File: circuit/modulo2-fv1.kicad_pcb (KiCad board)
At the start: 2 copper layers, 107 x 48 mm, 2 parts, among them J4 HOLE, J5 HOLE

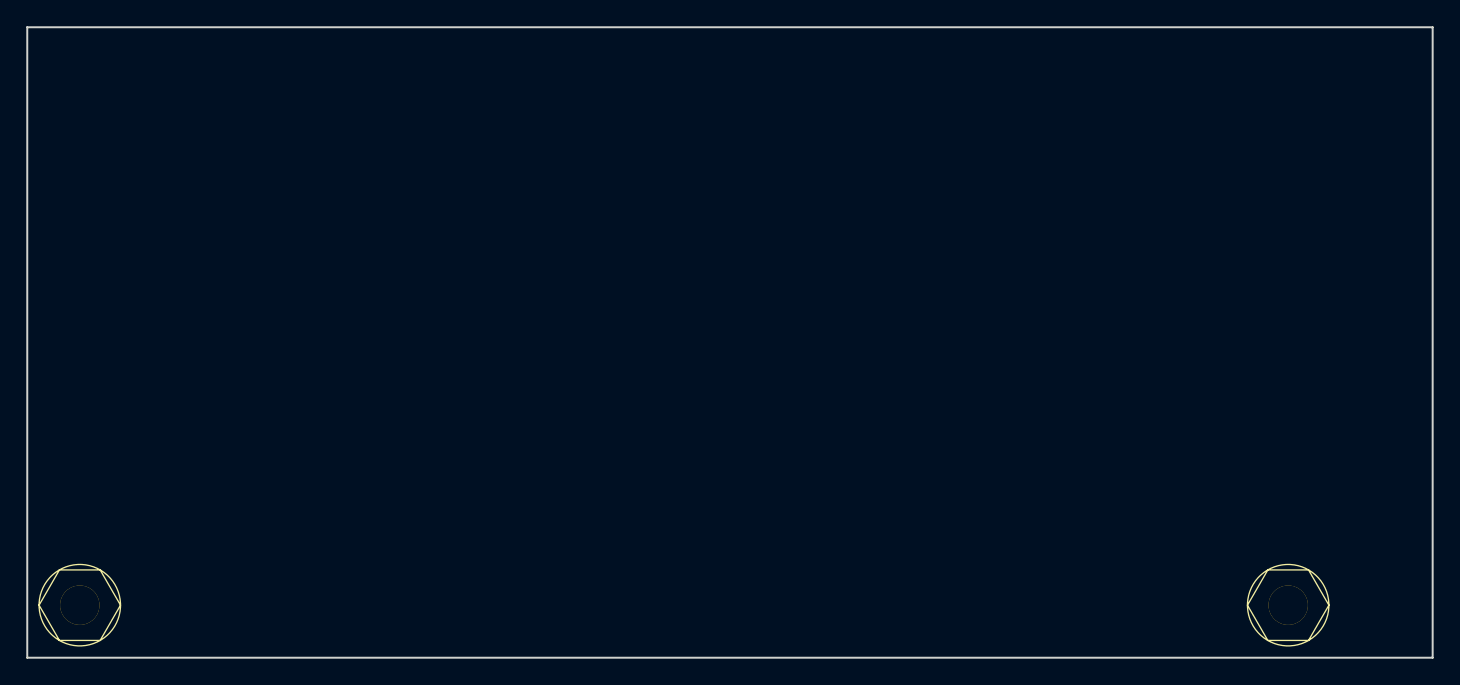
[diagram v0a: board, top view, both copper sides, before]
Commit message: made FV-1 prototype; converted kicad 5 files to kicad 6
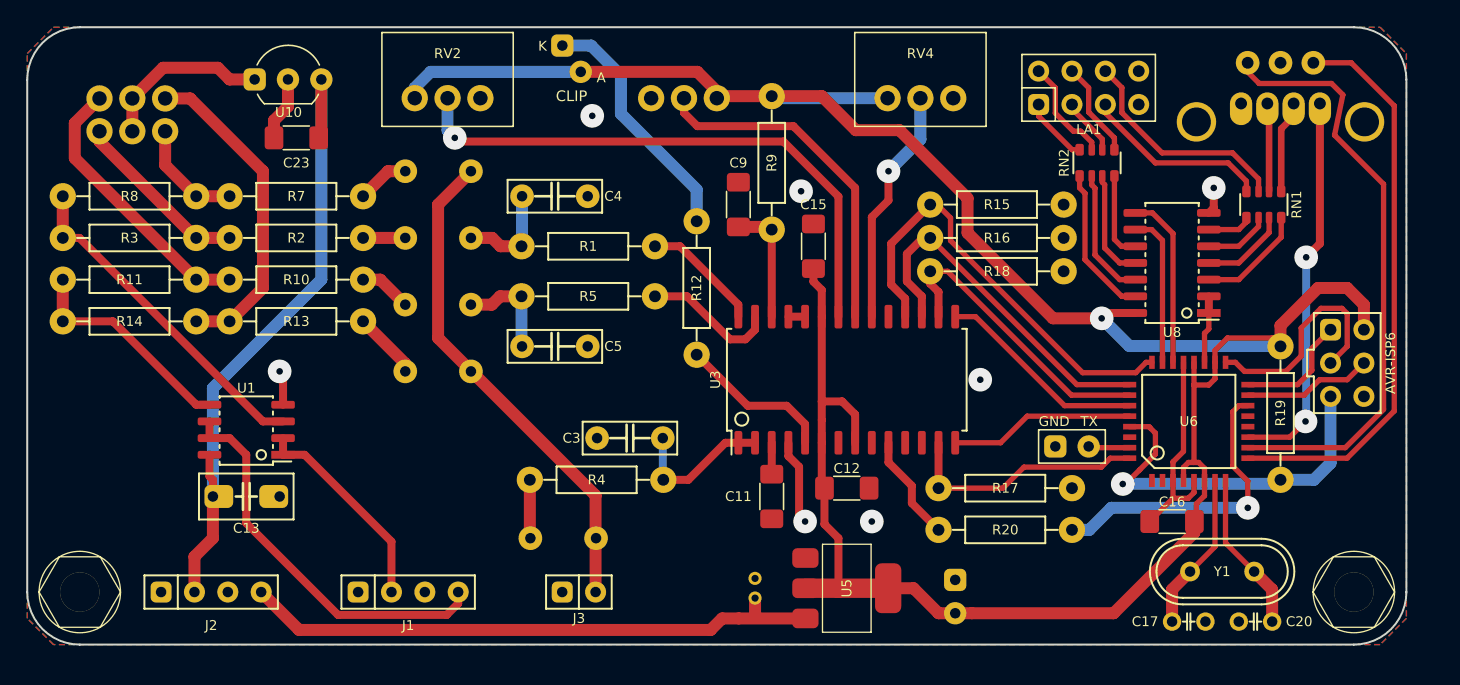
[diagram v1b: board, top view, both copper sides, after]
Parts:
- added C1: 1µF, myAmp:C_FILM_L7.2mm_W4.5mm_P5.00mm, B.Cu at (81.3, 66.0)
- added C10: 1µF, myAmp:C_FILM_L7.2mm_W4.5mm_P5.00mm, B.Cu at (81.3, 71.1)
- added C11: 1µF, myAmp:C_1206, F.Cu at (106.7, 85.7)
- added C12: 100nF, myAmp:C_1206, F.Cu at (112.4, 85.1)
- added C13: 100nF, myAmp:C_5MM_1206, F.Cu at (66.7, 85.7)
- added C14: 1µF, myAmp:C_FILM_L7.2mm_W4.5mm_P5.00mm, B.Cu at (81.3, 76.2)
- added C15: 100nF, myAmp:C_1206, F.Cu at (109.9, 66.7)
- added C16: 100n, myAmp:C_1206, F.Cu at (137.2, 87.6)
- added C17: 22p, myAmp:C_2.5MM, F.Cu at (138.4, 95.2)
- added C18: 10µF, myAmp:CPOL_D4_P1.5, B.Cu at (105.4, 92.7)
- added C19: 100µF, myAmp:CPOL_D6.3_P2.5, B.Cu at (120.7, 93.3)
- added C2: 1µF, myAmp:C_FILM_L7.2mm_W4.5mm_P5.00mm, B.Cu at (90.8, 88.9)
- added C20: 22p, myAmp:C_2.5MM, F.Cu at (143.5, 95.2)
- added C23: 100nF, myAmp:C_1206, F.Cu at (70.5, 58.4)
- added C3: 1nF, myAmp:C_FILM_L7.2mm_W2.5mm_P5.00mm, F.Cu at (95.9, 81.3)
- added C4: 10nF, myAmp:C_FILM_L7.2mm_W2.5mm_P5.00mm, F.Cu at (90.2, 62.9)
- added C5: 10nF, myAmp:C_FILM_L7.2mm_W2.5mm_P5.00mm, F.Cu at (90.2, 74.3)
- added C7: 1µF, myAmp:C_FILM_L7.2mm_W4.5mm_P5.00mm, B.Cu at (81.3, 61.0)
- added C9: 1µF, myAmp:C_1206, F.Cu at (104.1, 63.5)
- added D1: CLIP, myAmp:LED_D3.0mm_PCBedge, F.Cu at (91.4, 50.4)
- added J1: CONN_01X04, myAmp:PIN_1x04, F.Cu at (79.0, 93.0)
- added J2: CONN_01X04, myAmp:PIN_1x04, F.Cu at (64.0, 93.0)
- added J3: CONN_01X02, myAmp:PIN_1x02, F.Cu at (92.0, 93.0)
- added LA1: LED_ARRAY, myAmp:LED_ARRAY, F.Cu at (130.8, 54.6)
- added R1: 1K, myAmp:R_10MM, F.Cu at (92.7, 66.7)
- added R10: 10K, myAmp:R_10MM, F.Cu at (70.5, 69.2)
- added R11: 10K, myAmp:R_10MM, F.Cu at (57.8, 69.2)
- added R12: 100, myAmp:R_10MM, F.Cu at (101.0, 69.8)
- added R13: 10K, myAmp:R_10MM, F.Cu at (70.5, 72.4)
- added R14: 10K, myAmp:R_10MM, F.Cu at (57.8, 72.4)
- added R15: 10K, myAmp:R_10MM, F.Cu at (123.8, 63.5)
- added R16: 10K, myAmp:R_10MM, F.Cu at (123.8, 66.0)
- added R17: 10K, myAmp:R_10MM, F.Cu at (124.5, 85.1)
- added R18: 10K, myAmp:R_10MM, F.Cu at (123.8, 68.6)
- added R19: 10K, myAmp:R_10MM, F.Cu at (145.4, 79.4)
- added R2: 10K, myAmp:R_10MM, F.Cu at (70.5, 66.0)
- added R20: 10K, myAmp:R_10MM, F.Cu at (124.5, 88.3)
- added R3: 10K, myAmp:R_10MM, F.Cu at (57.8, 66.0)
- added R4: 1K, myAmp:R_10MM, F.Cu at (93.3, 84.5)
- added R5: 1K, myAmp:R_10MM, F.Cu at (92.7, 70.5)
- added R7: 10K, myAmp:R_10MM, F.Cu at (70.5, 62.9)
- added R8: 10K, myAmp:R_10MM, F.Cu at (57.8, 62.9)
- added R9: 100, myAmp:R_10MM, F.Cu at (106.7, 60.3)
- added RN1: 100, myAmp:R_Array_x4_1206, F.Cu at (144.1, 63.5)
- added RN2: 100, myAmp:R_Array_x4_1206, F.Cu at (131.4, 60.3)
- added RV1: B10K, myAmp:BOURNS_PTD902_xx15K, B.Cu at (58.0, 57.9)
- added RV2: 50K, myAmp:BOURNS_PTD901_xx15K, F.Cu at (82.0, 55.4)
- added RV3: 50K, myAmp:BOURNS_PTD901_xx15K, B.Cu at (100.0, 55.4)
- added RV4: 50K, myAmp:BOURNS_PTD901_xx15K, F.Cu at (118.0, 55.4)
- added SW1: ROTENC_BOURNS_PEL12D, myAmp:BOURNS_PEL12D-2xxx, B.Cu at (145.4, 52.7)
- added U1: NE5532, myAmp:SOIC-8_3.9x4.9mm_P1.27mm, F.Cu at (66.7, 80.6)
- added U10: TLE2426, myAmp:TO-92_Inline_Wide, F.Cu at (69.8, 54.0)
- added U3: FV-1, myAmp:SOIC-28_7.5x17.9mm_Pitch1.27mm, F.Cu at (112.4, 76.8)
- added U4: AVR-ISP6, myAmp:AVR_ISP6, F.Cu at (150.5, 75.6)
- added U5: LM1117 3V3, myAmp:SOT-223, F.Cu at (112.4, 92.7)
- added U6: ATmega328p, myAmp:TQFP-32_7x7mm_Pitch0.8mm, F.Cu at (138.4, 80.0)
- added U7: DBG_UART, myAmp:DBG_UART, F.Cu at (129.5, 81.9)
- added U8: 74164, myAmp:SOIC-14_3.9x8.7mm_P1.27mm, F.Cu at (137.2, 67.9)
- added Y1: 16MHz, myAmp:Crystal_HC49-U_Vertical, F.Cu at (141.0, 91.4)
- moved J4 5.10 mm to (151.0, 93.0)
- moved J5 1.00 mm to (54.0, 93.0)
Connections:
- J4 pad 1: (no net) -> unconnected-(J4-Pad1)
- J5 pad 1: (no net) -> unconnected-(J5-Pad1)
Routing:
- net +3V3: track 0.00 -> 189.6 mm, vias 0 -> 1
- net +24V: track 0.00 -> 50.8 mm
- net /ROT_A: track 0.00 -> 45.8 mm
- net +5V: track 0.00 -> 44.5 mm
- net Net-(RV2-Pad2): track 0.00 -> 43.5 mm, vias 0 -> 1
- net /ROT_B: track 0.00 -> 43.4 mm
- net IN: track 0.00 -> 38.1 mm
- net /S2: track 0.00 -> 33.7 mm
- net GND: track 0.00 -> 33.3 mm, vias 0 -> 7
- net /OUTR: track 0.00 -> 30.1 mm
- net /ROT_SW: track 0.00 -> 29.5 mm, vias 0 -> 2
- net /AVR_RST: track 0.00 -> 28.8 mm, vias 0 -> 1
- net /S1: track 0.00 -> 27.3 mm
- net Net-(RV3-Pad2): track 0.00 -> 26.3 mm
- net Net-(R3-Pad2): track 0.00 -> 25.7 mm
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- added copper zone on B.Cu, net GND
- added copper zone on F.Cu, net GND
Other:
- board size 107 x 48 mm -> 105 x 47 mm
- net class Default removed

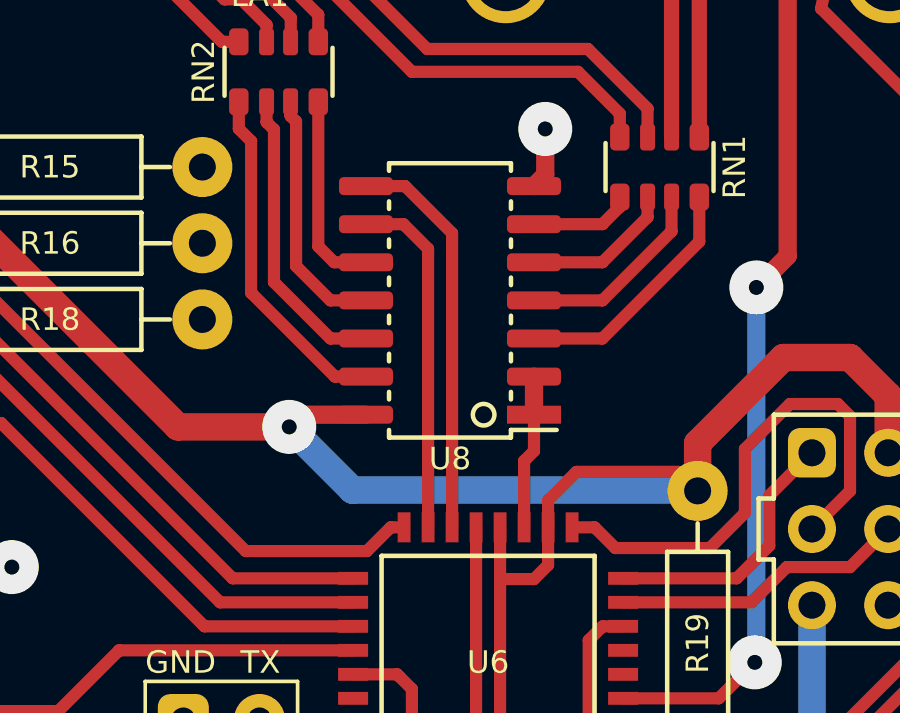
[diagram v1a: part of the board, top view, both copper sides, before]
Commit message: FV-1 firmware reworked for the new board; FV-1 PCB needs rework to correct errors
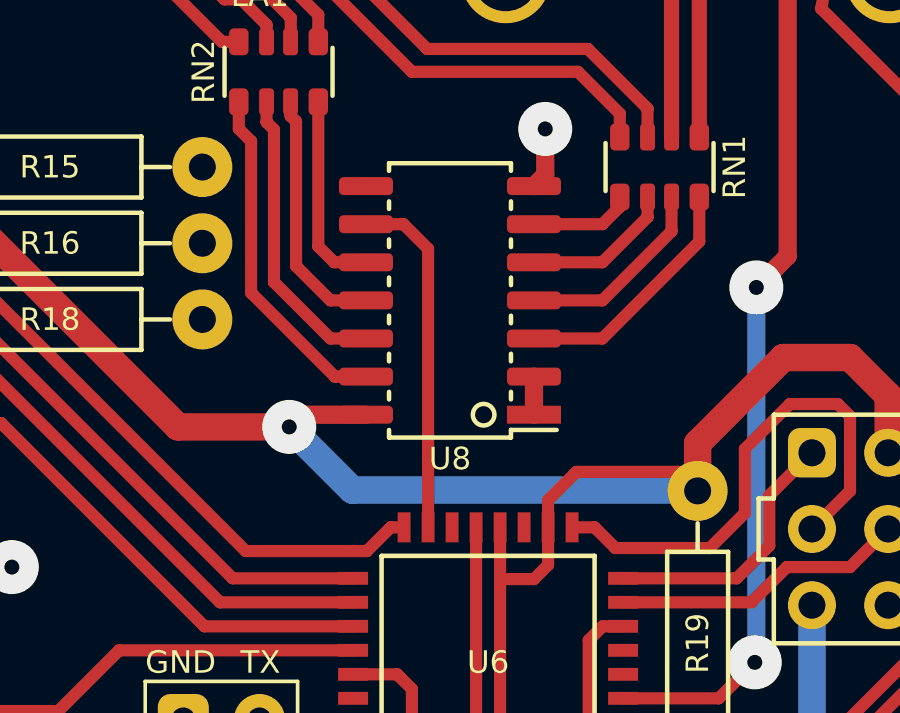
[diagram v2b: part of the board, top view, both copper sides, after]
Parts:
- C16: value 100n -> 100nF
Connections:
- U6 pad 12: unconnected-(U6-Pad12) -> /LED_CK
- U6 pad 13: unconnected-(U6-Pad13) -> /LED_DT
- U6 pad 19: /LED_DT -> unconnected-(U6-Pad19)
- U6 pad 22: /LED_CK -> unconnected-(U6-Pad22)
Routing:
- net /LED_CK: track 13.3 -> 0.00 mm
- net /LED_DT: track 5.16 -> 1.27 mm
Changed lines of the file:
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@@
   (net 62 "Net-(R20-Pad1)")
   (net 63 "unconnected-(U6-Pad1)")
-  (net 64 "unconnected-(U6-Pad12)")
-  (net 65 "unconnected-(U6-Pad13)")
+  (net 64 "unconnected-(U6-Pad19)")
+  (net 65 "unconnected-(U6-Pad22)")
   (net 66 "unconnected-(U6-Pad2)")
   (net 67 "Net-(LA1-Pad2)")
@@
       (net 48 "/ROT_SW") (pinfunction "(AIN1)PD7") (pintype "bidirectional"))
     (pad "12" smd rect (at -0.4 4.5 90) (size 0.43 1) (layers "F.Cu" "F.Paste" "F.Mask")
-      (net 64 "unconnected-(U6-Pad12)") (pinfunction "(ICP)PB0") (pintype "bidirectional+no_connect"))
+      (net 57 "/LED_CK") (pinfunction "(ICP)PB0") (pintype "bidirectional"))
     (pad "13" smd rect (at 0.4 4.5 90) (size 0.43 1) (layers "F.Cu" "F.Paste" "F.Mask")
-      (net 65 "unconnected-(U6-Pad13)") (pinfunction "(OC1A)PB1") (pintype "bidirectional+no_connect"))
+      (net 56 "/LED_DT") (pinfunction "(OC1A)PB1") (pintype "bidirectional"))
     (pad "14" smd rect (at 1.2 4.5 90) (size 0.43 1) (layers "F.Cu" "F.Paste" "F.Mask")
       (net 50 "/FV_CLK") (pinfunction "(~{SS}/OC1B)PB2") (pintype "bidirectional"))
@@
       (net 11 "+3V3") (pinfunction "AVCC") (pintype "power_in"))
     (pad "19" smd rect (at 4.5 1.2 90) (size 1 0.43) (layers "F.Cu" "F.Paste" "F.Mask")
-      (net 56 "/LED_DT") (pinfunction "ADC6") (pintype "bidirectional"))
+      (net 64 "unconnected-(U6-Pad19)") (pinfunction "ADC6") (pintype "bidirectional+no_connect"))
     (pad "20" smd rect (at 4.5 0.4 90) (size 1 0.43) (layers "F.Cu" "F.Paste" "F.Mask")
       (net 11 "+3V3") (pinfunction "AREF") (pintype "bidirectional"))
@@
       (net 5 "GND") (pinfunction "AGND") (pintype "power_in"))
     (pad "22" smd rect (at 4.5 -1.2 90) (size 1 0.43) (layers "F.Cu" "F.Paste" "F.Mask")
-      (net 57 "/LED_CK") (pinfunction "ADC7") (pintype "bidirectional"))
+      (net 65 "unconnected-(U6-Pad22)") (pinfunction "ADC7") (pintype "bidirectional+no_connect"))
     (pad "23" smd rect (at 4.5 -2 90) (size 1 0.43) (layers "F.Cu" "F.Paste" "F.Mask")
       (net 58 "/LED_RST") (pinfunction "(ADC0)PC0") (pintype "bidirectional"))
@@
       (effects (font (size 0.75 0.75) (thickness 0.15)))
     )
-    (fp_text value "100n" (at 0.0127 0.5715) (layer "Dwgs.User") hide
+    (fp_text value "100nF" (at 0.0127 0.5715) (layer "Dwgs.User") hide
       (effects (font (size 0.127 0.127) (thickness 0.001)))
     )
@@
   (segment (start 147.2118 78.01) (end 142.93 78.01) (width 0.4064) (layer "F.Cu") (net 55))
   (segment (start 151.765 75.565) (end 150.495 76.835) (width 0.4064) (layer "F.Cu") (net 55))
-  (segment (start 139.63 75.51) (end 139.63 73.2982) (width 0.4064) (layer "F.Cu") (net 56))
-  (segment (start 139.63 73.2982) (end 139.96 72.9682) (width 0.4064) (layer "F.Cu") (net 56))
   (segment (start 139.96 70.485) (end 139.96 71.755) (width 0.6096) (layer "F.Cu") (net 56))
-  (segment (start 139.96 72.9682) (end 139.96 71.755) (width 0.4064) (layer "F.Cu") (net 56))
-  (segment (start 137.23 65.7036) (end 135.6614 64.135) (width 0.4064) (layer "F.Cu") (net 57))
-  (segment (start 137.23 75.51) (end 137.23 65.7036) (width 0.4064) (layer "F.Cu") (net 57))
-  (segment (start 135.6614 64.135) (end 134.36 64.135) (width 0.4064) (layer "F.Cu") (net 57))
   (segment (start 136.43 75.51) (end 136.43 66.2244) (width 0.4064) (layer "F.Cu") (net 58))
   (segment (start 135.6106 65.405) (end 134.36 65.405) (width 0.4064) (layer "F.Cu") (net 58))

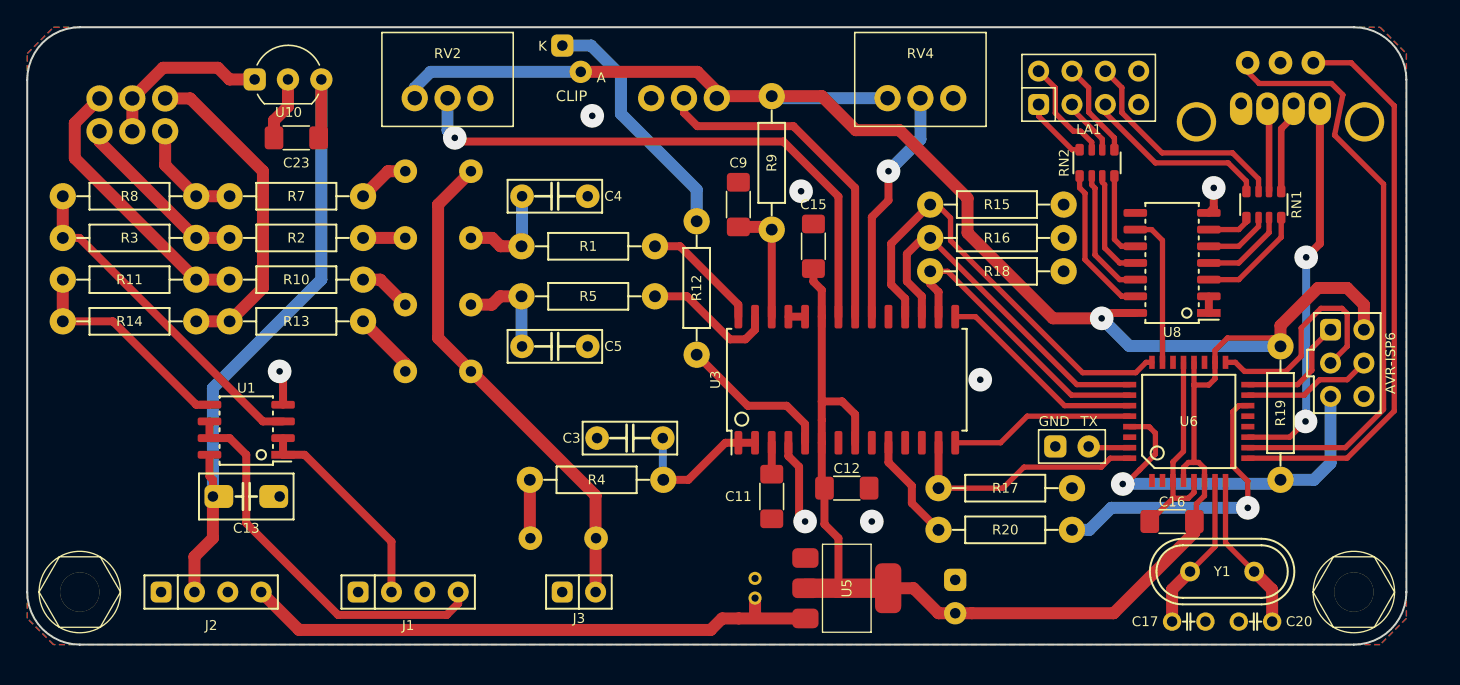
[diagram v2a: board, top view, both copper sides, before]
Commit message: added report on createBanks.py; started PCB redesign
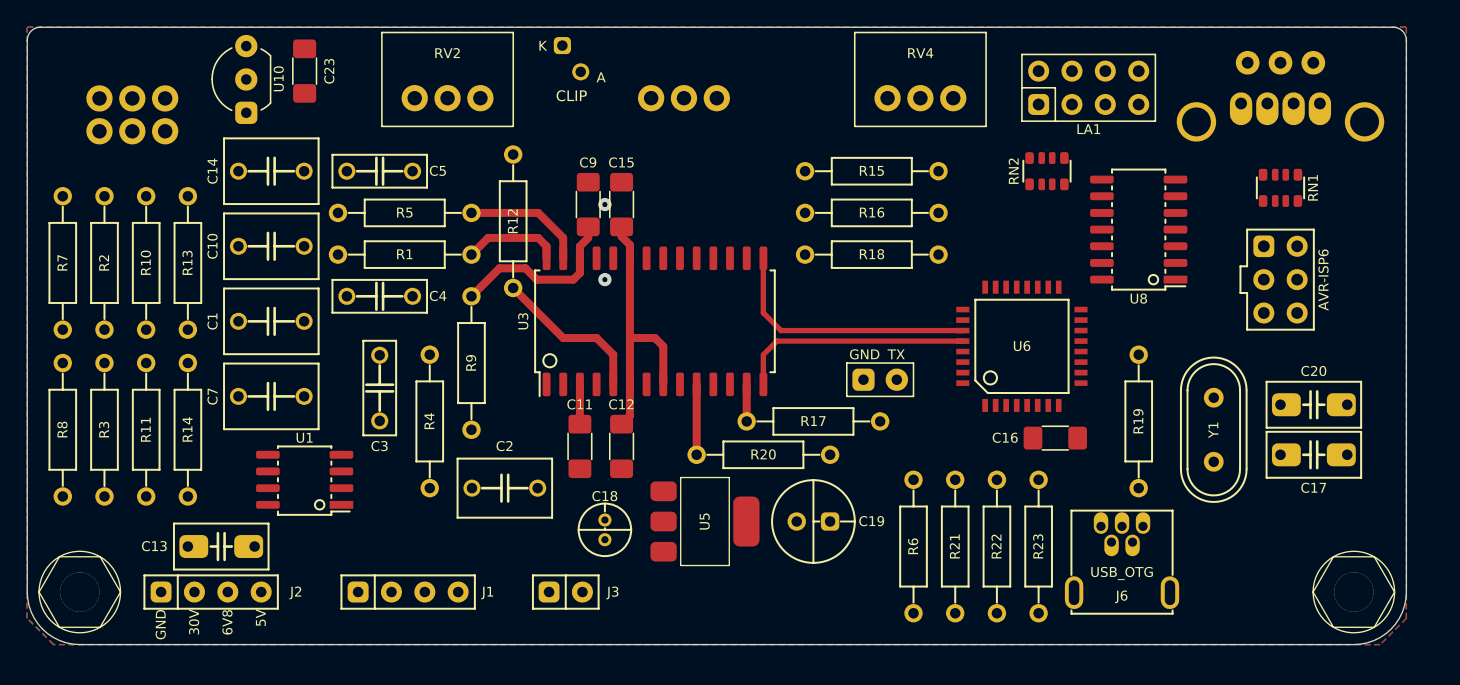
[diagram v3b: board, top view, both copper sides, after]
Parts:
- added J6: USB_OTG, myAmp:USB_OTG_THT, F.Cu at (133.3, 88.0)
- added R21: 68, myAmp:R_10MM, F.Cu at (120.7, 89.5)
- added R22: 68, myAmp:R_10MM, F.Cu at (123.8, 89.5)
- added R23: 1K5, myAmp:R_10MM, F.Cu at (127.0, 89.5)
- added R6: 1K5, myAmp:R_10MM, F.Cu at (117.5, 89.5)
- C1, C10, C14, C7: footprint myAmp:C_FILM_L7.2mm_W4.5mm_P5.00mm -> myAmp:C_FILM_L7.2mm_W5.0mm_P5.00mm; moved to F.Cu
- C17, C20: footprint myAmp:C_2.5MM -> myAmp:C_5MM_1206
- C18, C19, C2: moved to F.Cu
- J2: value CONN_01X04 -> POWER; footprint myAmp:PIN_1x04 -> myAmp:POWER
- moved R9 27.5 mm to (83.8, 75.6), turned to 90 degrees
- moved C7 21.3 mm to (68.6, 78.1)
- moved C14 19.8 mm to (68.6, 61.0)
- moved C3 19.4 mm to (76.8, 77.5), turned to 90 degrees
- moved R20 19.3 mm to (106.0, 82.5)
- moved C5 18.9 mm to (76.8, 61.0)
- moved R7 18.5 mm to (52.7, 67.9), turned to -90 degrees
- moved R8 18.5 mm to (52.7, 80.6), turned to -90 degrees
- moved C12 17.4 mm to (95.2, 81.9), turned to -90 degrees
- moved C20 17.1 mm to (148.0, 78.7), turned to 0 degrees
- moved C17 15.9 mm to (148.0, 82.5)
- moved U7 15.5 mm to (114.9, 76.8)
- moved R17 15.5 mm to (109.9, 80.0)
- moved C4 15.4 mm to (76.8, 70.5)
- moved R5 15.3 mm to (78.7, 64.1)
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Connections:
- U6 pad 1: unconnected-(U6-Pad1) -> /D-
- U6 pad 12: /LED_CK -> unconnected-(U6-Pad12)
- U6 pad 13: /LED_DT -> unconnected-(U6-Pad13)
- U6 pad 30: unconnected-(U6-Pad30) -> /T0
- U6 pad 32: /T0 -> /D+
- U8 pad 1: /LED_DT -> /MOSI
- U8 pad 2: /LED_DT -> /MOSI
- U8 pad 8: /LED_CK -> /SCK
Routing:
- net +3V3: track 189.6 -> 21.2 mm, vias 1 -> 0
- net +24V: track 50.8 -> 0.00 mm
- net /ROT_A: track 45.8 -> 0.00 mm
- net +5V: track 44.5 -> 0.00 mm
- net Net-(RV2-Pad2): track 43.5 -> 0.00 mm, vias 1 -> 0
- net /ROT_B: track 43.4 -> 0.00 mm
- net IN: track 38.1 -> 0.00 mm
- net /S2: track 33.7 -> 0.00 mm
- net GND: track 33.3 -> 0.00 mm, vias 7 -> 2
- net /OUTR: track 30.1 -> 0.00 mm
- net /ROT_SW: track 29.5 -> 0.00 mm, vias 2 -> 0
- net /AVR_RST: track 28.8 -> 0.00 mm, vias 1 -> 0
- net /S1: track 27.3 -> 0.00 mm
- net Net-(RV3-Pad2): track 26.3 -> 0.00 mm
- net Net-(R3-Pad2): track 25.7 -> 0.00 mm
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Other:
- outline, holes or cut-outs redrawn
